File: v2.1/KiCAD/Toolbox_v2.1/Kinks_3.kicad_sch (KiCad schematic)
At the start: 31 parts, among them J30 Kinks_OUT_Noise, J31 Kinks_OUT_S&H, J32 Kinks_S&H_IN, J33 Kinks_S&H_TRIG, Q1 MMBT3904, Q2 MMBT3904, Q3 MMBFJ310, U11 TL074, U7 TL074

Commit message: v2.1 Update
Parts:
- added C39: 22pF, Capacitor_SMD:C_0603_1608Metric, symbol Device:C
- added C43: 0.01uF/16V, Capacitor_SMD:C_0805_2012Metric_Pad1.18x1.45mm_HandSolder, symbol Device:C
- added J30: Jumper, Connector_PinHeader_2.54mm:PinHeader_1x03_P2.54mm_Vertical, symbol Connector:Conn_01x03_Pin
- added R94: 2.2K, Resistor_SMD:R_0603_1608Metric, symbol Device:R
- added R95: 2K, Resistor_SMD:R_0603_1608Metric, symbol Device:R
- added R96: 100R, Resistor_SMD:R_0402_1005Metric, symbol Device:R
- added U14: TL072CDT, Package_SO:SOIC-8_3.9x4.9mm_P1.27mm, symbol Amplifier_Operational:TL072
- C40: renamed from C41; value 100nF -> 0.1uF/16V; footprint Capacitor_THT:C_Rect_L7.2mm_W2.5mm_P5.00mm_FKS2_FKP2_MKS2_MKP2 -> Capacitor_SMD:C_1210_3225Metric_Pad1.33x2.70mm_HandSolder
- Q1, Q2: value MMBT3904 -> 2SC1815; LCSC C20526 -> C20069143
- Q3: LCSC (none) -> C33416
- U11, U7: value TL074 -> TL074CDR; footprint Package_SO:TSSOP-14_4.4x5mm_P0.65mm -> Package_SO:SOIC-14_3.9x8.7mm_P1.27mm; LCSC C4370424 -> C12594
- renumbered C42 to C41, C43 to C42, J30 to J31, J31 to J32, J32 to J33, J33 to J34, R99 to R100, R100 to R102, R102 to R103, R103 to R104, R104 to R105, R91 to R89, R92 to R90, R93 to R91, R94 to R92, R95 to R93, R96 to R97, R97 to R98, R98 to R99
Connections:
- net GND: now also U14.3 (+), U14.5 (+)
- net at R91.2, R93.1: now also C39.2, R95.1, U14.1; no longer U11.8
- net NOISE: now reaches J31.T, J33.TN
- net NOISE: now also J30.2 (Pin_2); no longer R93.2
- net at R91.1, R92.2: now also C39.1, U14.2 (-); no longer U11.9 (-)
- new net: R94.2, R96.1, U14.7
- new net: J30.3 (Pin_3), R96.2
- new net: C43.1, R95.2
- new net: J30.1 (Pin_1), R93.2
- new net: U11.8, U11.9 (-)
- new net: C43.2, R94.1, U14.6 (-)
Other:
- note added: "ECHU1C103JX5"
- note added: "ECHU1C104JX5"
- note removed: "- 22pF並列 -"
- note removed: "ノイズ周りだけオペアンプ分けたほうがいいかも rev2で対応予定"
- moved on the sheet: C40, C41, C42, C44, C45, D20, D21, D22, J31, J32, J33, J34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

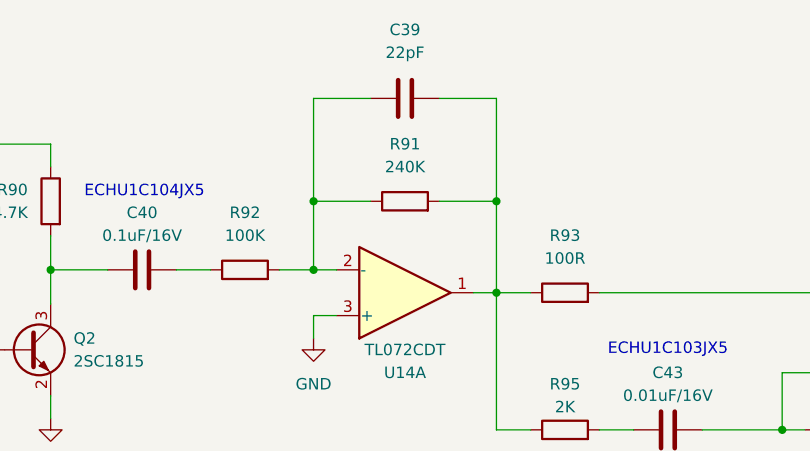
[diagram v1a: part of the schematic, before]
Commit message: R91 定数変更 240K→200K
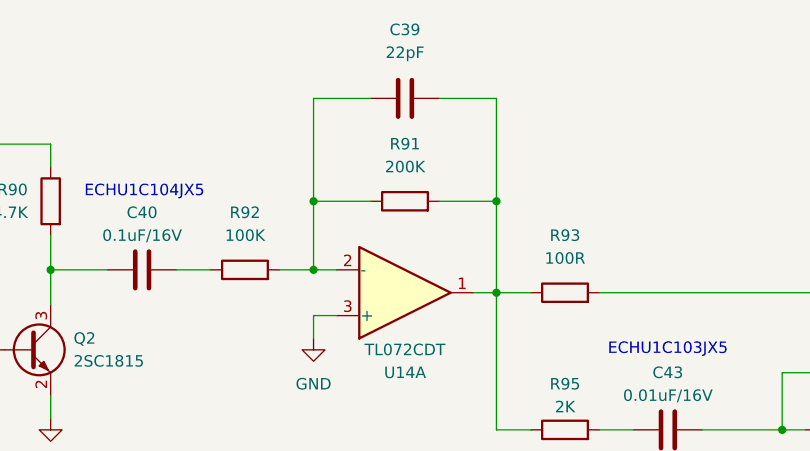
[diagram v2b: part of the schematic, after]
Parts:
- R91: value 240K -> 200K; LCSC C4197 -> C25811
